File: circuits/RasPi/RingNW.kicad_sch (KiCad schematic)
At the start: 18 parts, among them J1 Conn_01x14_Pin, SW1 SW_SPST, U1 STM32F446RETx, Y1 16MHz

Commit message: ラズパイ基板とか
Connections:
- net BOOT0 renamed BOOT
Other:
- sheet UI_RingNW ports: added DIPSW0, DIPSW1, DIPSW2, DIPSW3, SlideSW0; removed DIP_SW0, DIP_SW1, DIP_SW2, DIP_SW3, Slide_SW0

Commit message: PDFプロット
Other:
- sheet UI_RingNW ports: added LED_B0, LED_B1, LED_LG0, LED_Y0, LED_nR0; removed LED0, LED1
- note added: "MOSI/MISOはいつものとおんなじでいいのか いつもはマスターだけど今回はスレーブ H723VGにする"

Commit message: panelフットプリント配置
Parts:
- added C20: 4.7uF, Capacitor_SMD:C_0603_1608Metric, symbol Device:C
- added C22: 1uF, Capacitor_SMD:C_0402_1005Metric, symbol Device:C
- added U15: STM32H723VGTx, Package_QFP:LQFP-100_14x14mm_P0.5mm, symbol MCU_ST_STM32H7:STM32H723VGTx
- U1: footprint Package_QFP:LQFP-64_10x10mm_P0.5mm -> (none)
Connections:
- net +3.3V: now also C22.2, U15.100 (VDD), U15.11 (VDD), U15.21 (VDDA), U15.27 (VDD), U15.50 (VDD), U15.6 (VBAT), U15.75 (VDD)
- net BOOT: now also U15.94 (BOOT0)
- net GNDD: now also C20.2, C22.1, U15.10 (VSS), U15.19 (VSSA), U15.26 (VSS), U15.49 (VSS), U15.74 (VSS), U15.99 (VSS)
- net HSE_IN: now also U15.12 (PH0)
- net HSE_OUT: now also U15.13 (PH1)
- net NRST: now also U15.14 (NRST)
- new net: C20.1, U15.73 (VCAP)
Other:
- note added: "MOSI/MISOはいつものとおんなじでいいのか いつもはマスターだけど今回はスレーブ"
- note removed: "MOSI/MISOはいつものとおんなじでいいのか いつもはマスターだけど今回はスレーブ H723VGにする"
- moved on the sheet: C1, C10, C2, C3, C4, C5, C6, C7, C8, C9, D1, J1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

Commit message: シンボル・フットプリントMyLib->TomoshibiLib置き換え
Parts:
- J1: footprint MyLibrary:BoxHeader_2x07_P1.27mm_Horizontal -> TomoshibiLibrary:BoxHeader_2x07_P1.27mm_Horizontal

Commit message: 更新
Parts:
- removed C10: 1uF, Capacitor_SMD:C_0402_1005Metric, symbol Device:C
- removed C9: 4.7uF, Capacitor_SMD:C_0603_1608Metric, symbol Device:C
- removed R3: 10k, Resistor_SMD:R_0402_1005Metric, symbol Device:R
- removed U1: STM32F446RETx, symbol MCU_ST_STM32F4:STM32F446RETx
- added C19, C62: 2.2uF, Capacitor_SMD:C_0402_1005Metric, symbol Device:C
- added C63: 1uF, Capacitor_SMD:C_0402_1005Metric, symbol Device:C
- C22: value 1uF -> 0.1uF
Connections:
- net +3.3V: now also C20.1, C22.1, U15.20 (VREF+), C63.1; no longer C22.2
- net GNDD: now also C22.2, C19.2, C62.2, C63.2; no longer C22.1
- net SWCLK: now also U15.76 (PA14(JTCK)
- net SWDIO: now also U15.72 (PA13(JTMS)
- net SWO: now also U15.89 (PB3(JTDO)
- net at U15.48 (VCAP): now also C19.1
- net at U15.73 (VCAP): now also C62.1; no longer C20.1
- net BOOT renamed BOOT0
- no-connect marks 11 -> 12
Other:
- note added: "H723VG"
- note removed: "F446RE"
- moved on the sheet: C1, C20, C3, C6, C7, C8

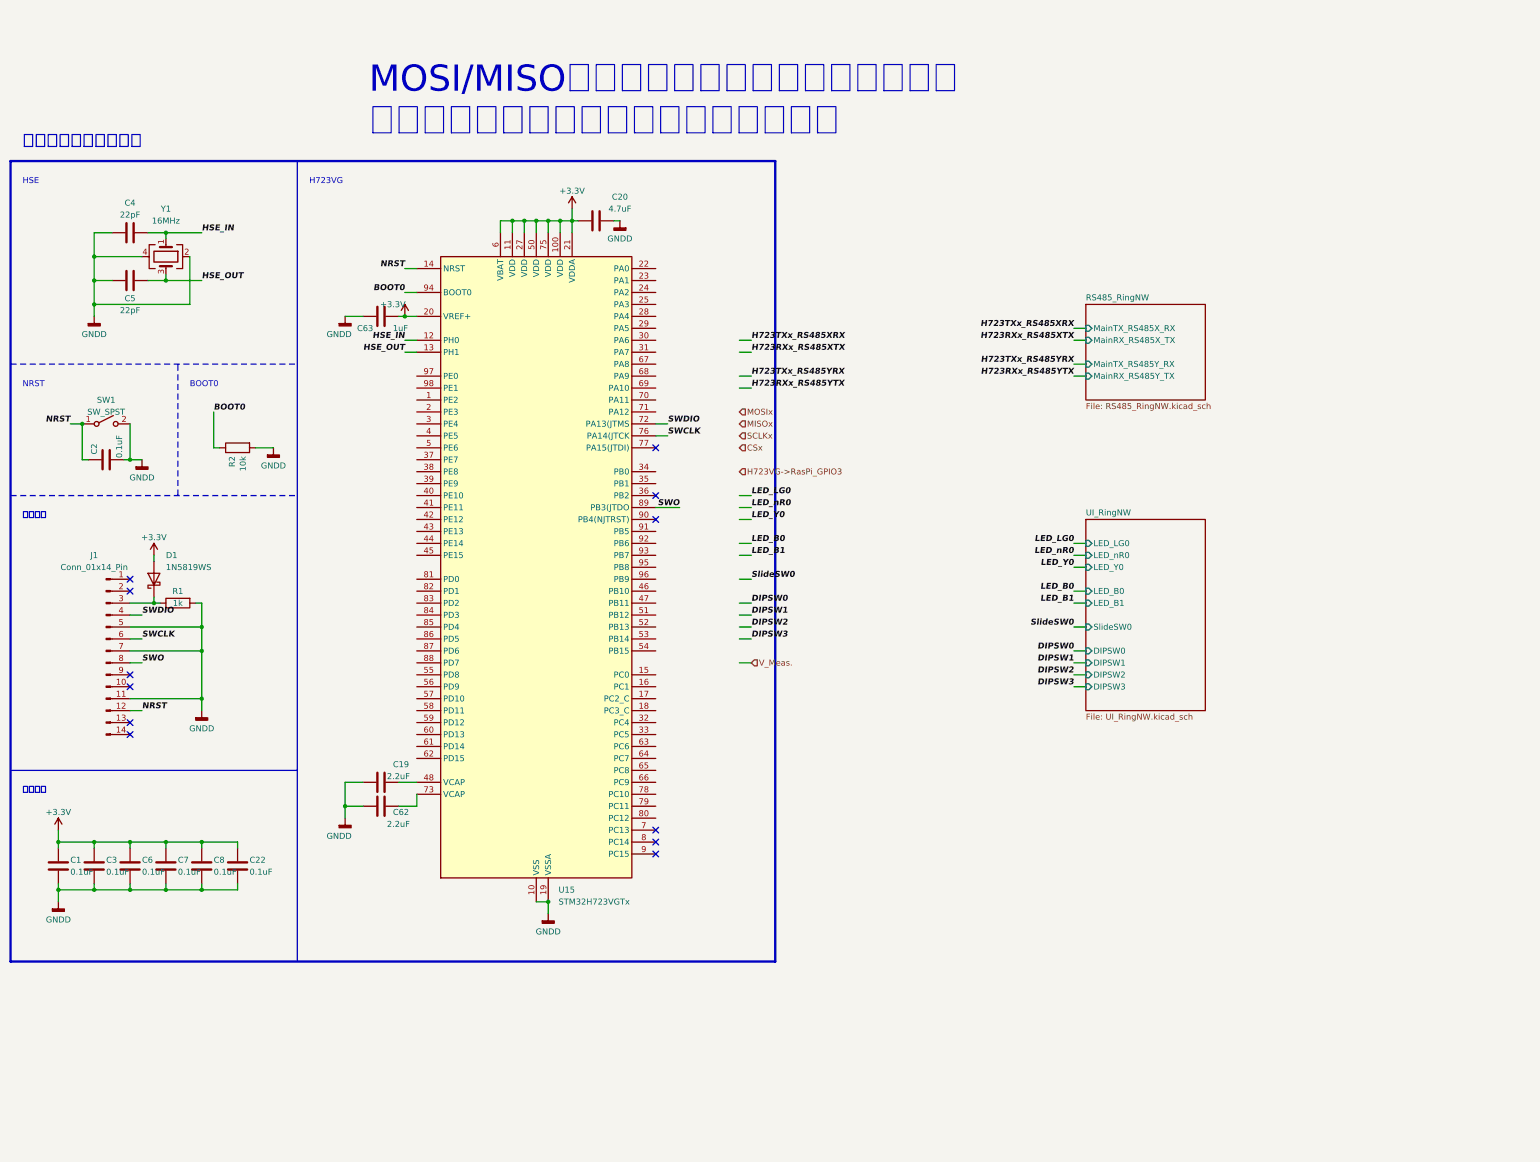
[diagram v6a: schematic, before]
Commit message: 発注第2弾
RasPi発注
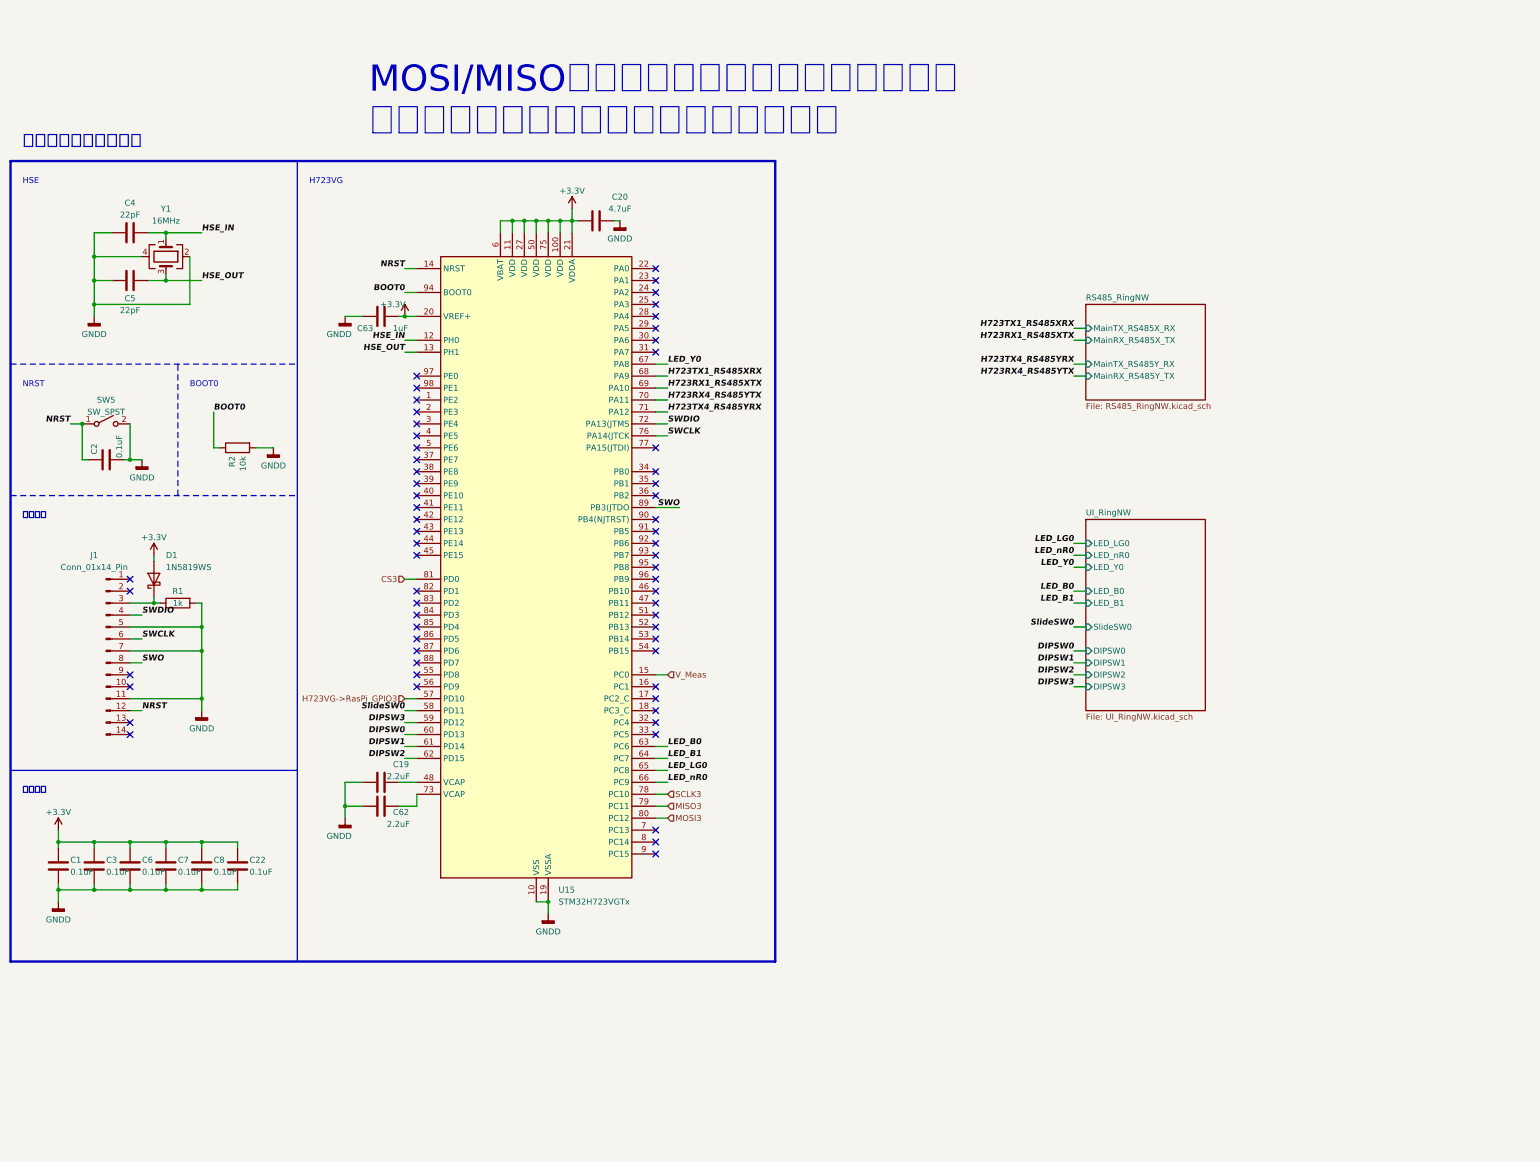
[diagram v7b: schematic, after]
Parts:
- D1: footprint Diode_SMD:D_SOD-323_HandSoldering -> TomoshibiLibrary:Diode_SOD-323
- renumbered SW1 to SW5
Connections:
- net DIPSW0: now also U15.60 (PD13)
- net DIPSW1: now also U15.61 (PD14)
- net DIPSW2: now also U15.62 (PD15)
- net DIPSW3: now also U15.59 (PD12)
- net H723VG->RasPi_GPIO3: now also U15.57 (PD10)
- net LED_B0: now also U15.63 (PC6)
- net LED_B1: now also U15.64 (PC7)
- net LED_LG0: now also U15.65 (PC8)
- net LED_Y0: now also U15.67 (PA8)
- net LED_nR0: now also U15.66 (PC9)
- net SlideSW0: now also U15.58 (PD11)
- net V_Meas: now reaches U15.15 (PC0)
- net H723TX1_RS485XRX: now reaches U15.68 (PA9)
- net H723RX1_RS485XTX: now reaches U15.69 (PA10)
- net H723RX4_RS485YTX: now reaches U15.70 (PA11)
- net H723TX4_RS485YRX: now reaches U15.71 (PA12)
- net SCLK3: now reaches U15.78 (PC10)
- net MISO3: now reaches U15.79 (PC11)
- net MOSI3: now reaches U15.80 (PC12)
- net CS3: now reaches U15.81 (PD0)
- no-connect marks 12 -> 63
